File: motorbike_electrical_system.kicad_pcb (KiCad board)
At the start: 2 copper layers, 101.9 x 82.9 mm, 70 parts, among them IC2 BDX34C, IC3 BDX34C, K1 RT42xxxx, Q1 D45VH10, Q10 BC337, Q11 BC337, Q12 BC327, Q13 BC337, Q14 D45VH10, Q15 D45VH10, Q2 D45VH10, Q3 BC337, Q4 BC337, Q5 BC337, Q6 BC337, Q7 BC337, Q8 BC337, Q9 BC337, U1 L7805, U2 L7805, U3 L7805, U4 ATmega16L-8P

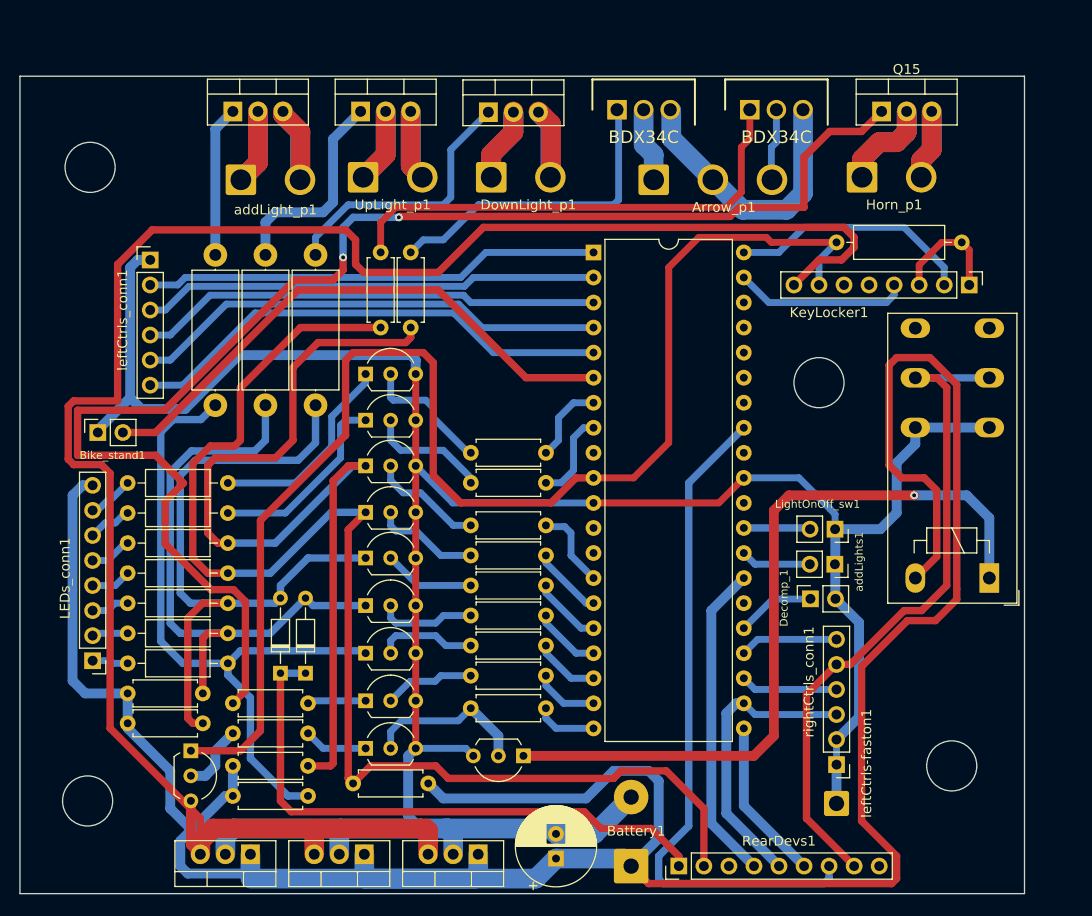
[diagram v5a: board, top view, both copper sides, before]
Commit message: fix: missing Vy(1,2) references for the key authentication
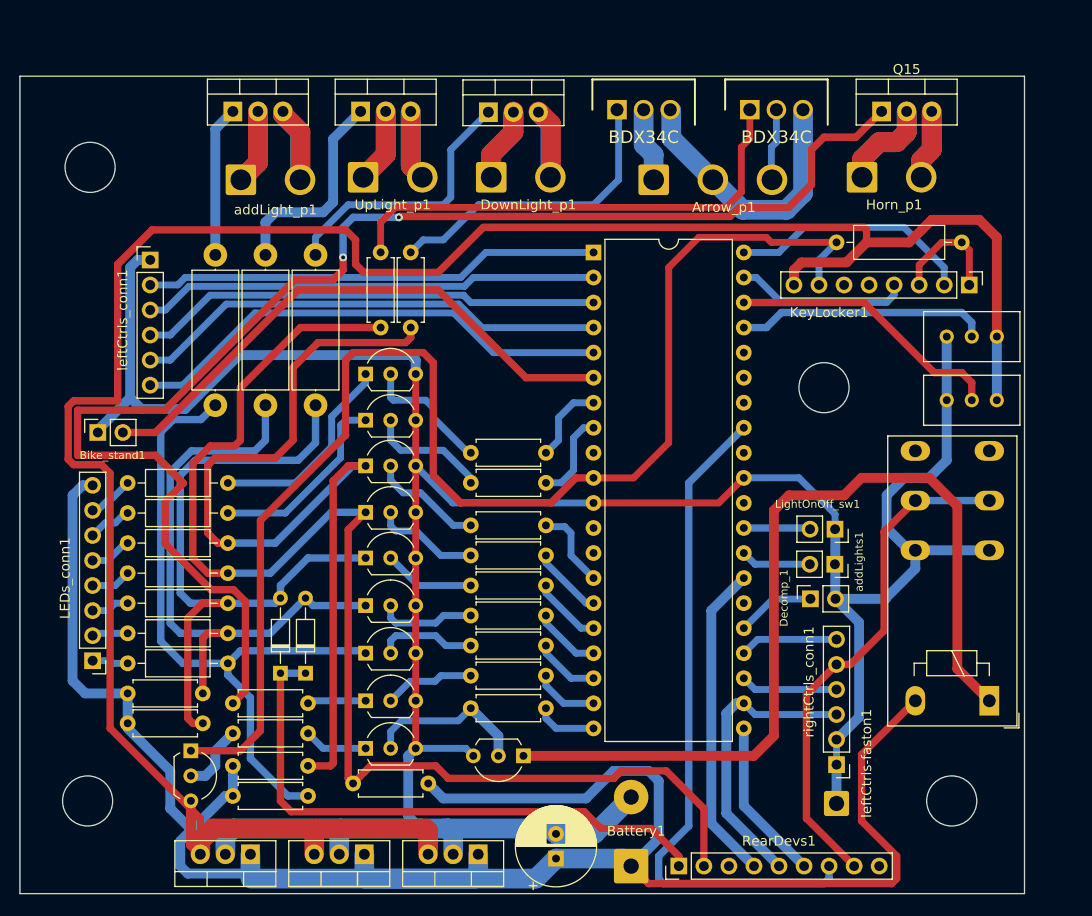
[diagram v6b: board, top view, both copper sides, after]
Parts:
- added RV1: 10K, Potentiometer_THT:Potentiometer_Bourns_3296W_Vertical, F.Cu at (208.0, 88.5)
- added RV2: 10K, Potentiometer_THT:Potentiometer_Bourns_3296W_Vertical, F.Cu at (208.0, 82.1)
- moved K1 12.4 mm to (207.3, 119.0)
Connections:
- U4 pad 37: unconnected-(U4-Pad37) -> Net-(U4-Pad37)
- U4 pad 38: unconnected-(U4-Pad38) -> Net-(U4-Pad38)
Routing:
- net +12V: track 276.9 -> 207.3 mm
- net +5V: track 198.0 -> 233.0 mm
- net Net-(U4-Pad38): track 0.00 -> 28.3 mm
- net Net-(U4-Pad37): track 0.00 -> 25.6 mm
- net GND: track 259.5 -> 281.6 mm
- net c_engineOFF: track 69.4 -> 52.0 mm
- net Net-(K1-PadA1): track 78.6 -> 91.3 mm, vias 1 -> 0
- net Net-(IC3-Pad1): track 32.5 -> 31.3 mm
- net Net-(Q15-Pad1): track 144.4 -> 143.5 mm
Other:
- outline, holes or cut-outs redrawn
